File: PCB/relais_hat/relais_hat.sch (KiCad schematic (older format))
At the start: 61 parts, among them J1 Conn_01x03, J10 Conn_01x02, J11 Conn_01x02, J12 Conn_01x03, J13 DB9_Female, J14 Conn_01x02, J15 Conn_01x02, J16 Conn_01x02, J17 Conn_01x02, J18 Conn_01x02, J2 Conn_01x03, J3 Conn_02x04_Odd_Even, J4 Screw_Terminal_01x02, J5 Screw_Terminal_01x02, J6 Screw_Terminal_01x02, J7 Screw_Terminal_01x02, J8 Conn_01x02, J9 Conn_01x02, K1 RELAY-HLS8L-DC3V-S-C(5P-19X15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, K2 RELAY-HLS8L-DC3V-S-C(5P-19X15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, K3 RELAY-HLS8L-DC3V-S-C(5P-19X15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, K4 RELAY-HLS8L-DC3V-S-C(5P-19X15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, P1 Conn_02x20_Odd_Even, Q1 S8050, Q2 S8050, Q3 S8050, Q4 S8050, U1 XC6206P302MR-G, U2 XC6206P302MR-G, U3 XC6206P302MR-G, U4 XC6206P302MR-G

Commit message: ajust all board
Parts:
- D1, D2, D3, D4: footprint LED_SMD:LED_1206_3216Metric -> LED_SMD:LED_0805_2012Metric; LCSC C375461 -> C84256
- R10, R11, R12, R9: LCSC C102018 -> C17713
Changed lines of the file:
@@
 Sheet 1 1
 Title ""
-Date "15 nov 2012"
-Rev ""
+Date "2020-10-30"
+Rev "3.0"
 Comp ""
 Comment1 ""
@@
 F 0 "D2" V 4800 4550 50  0000 R CNN
 F 1 "LED" V 4700 4550 50  0000 R CNN
-F 2 "LED_SMD:LED_1206_3216Metric" H 4750 4350 50  0001 C CNN
+F 2 "LED_SMD:LED_0805_2012Metric" H 4750 4350 50  0001 C CNN
 F 3 "~" H 4750 4350 50  0001 C CNN
-F 4 "C375461" V 4750 4350 50  0001 C CNN "LCSC"
+F 4 "C84256" V 4750 4350 50  0001 C CNN "LCSC"
 	1    4750 4350
 	0    -1   -1   0
@@
 F 2 "Resistor_SMD:R_0805_2012Metric" V 4930 5300 50  0001 C CNN
 F 3 "~" H 5000 5300 50  0001 C CNN
-F 4 "C102018" V 5000 5300 50  0001 C CNN "LCSC"
+F 4 "C17713" V 5000 5300 50  0001 C CNN "LCSC"
 	1    5000 5300
 	0    -1   -1   0
@@
 F 0 "D3" V 1700 6700 50  0000 R CNN
 F 1 "LED" V 1600 6700 50  0000 R CNN
-F 2 "LED_SMD:LED_1206_3216Metric" H 1650 6500 50  0001 C CNN
+F 2 "LED_SMD:LED_0805_2012Metric" H 1650 6500 50  0001 C CNN
 F 3 "~" H 1650 6500 50  0001 C CNN
-F 4 "C375461" V 1650 6500 50  0001 C CNN "LCSC"
+F 4 "C84256" V 1650 6500 50  0001 C CNN "LCSC"
 	1    1650 6500
 	0    -1   -1   0
@@
 F 2 "Resistor_SMD:R_0805_2012Metric" V 1830 7450 50  0001 C CNN
 F 3 "~" H 1900 7450 50  0001 C CNN
-F 4 "C102018" V 1900 7450 50  0001 C CNN "LCSC"
+F 4 "C17713" V 1900 7450 50  0001 C CNN "LCSC"
 	1    1900 7450
 	0    -1   -1   0
@@
 F 0 "D1" V 1650 4700 50  0000 R CNN
 F 1 "LED" V 1550 4750 50  0000 R CNN
-F 2 "LED_SMD:LED_1206_3216Metric" H 1600 4550 50  0001 C CNN
+F 2 "LED_SMD:LED_0805_2012Metric" H 1600 4550 50  0001 C CNN
 F 3 "~" H 1600 4550 50  0001 C CNN
-F 4 "C375461" V 1600 4550 50  0001 C CNN "LCSC"
+F 4 "C84256" V 1600 4550 50  0001 C CNN "LCSC"
 	1    1600 4550
 	0    -1   -1   0
@@
 F 2 "Resistor_SMD:R_0805_2012Metric" V 1780 5500 50  0001 C CNN
 F 3 "~" H 1850 5500 50  0001 C CNN
-F 4 "C102018" V 1850 5500 50  0001 C CNN "LCSC"
+F 4 "C17713" V 1850 5500 50  0001 C CNN "LCSC"
 	1    1850 5500
 	0    -1   -1   0
@@
 F 0 "D4" V 4850 6800 50  0000 R CNN
 F 1 "LED" V 4750 6800 50  0000 R CNN
-F 2 "LED_SMD:LED_1206_3216Metric" H 4800 6600 50  0001 C CNN
+F 2 "LED_SMD:LED_0805_2012Metric" H 4800 6600 50  0001 C CNN
 F 3 "~" H 4800 6600 50  0001 C CNN
-F 4 "C375461" V 4800 6600 50  0001 C CNN "LCSC"
+F 4 "C84256" V 4800 6600 50  0001 C CNN "LCSC"
 	1    4800 6600
 	0    -1   -1   0
@@
 F 2 "Resistor_SMD:R_0805_2012Metric" V 4980 7550 50  0001 C CNN
 F 3 "~" H 5050 7550 50  0001 C CNN
-F 4 "C102018" V 5050 7550 50  0001 C CNN "LCSC"
+F 4 "C17713" V 5050 7550 50  0001 C CNN "LCSC"
 	1    5050 7550
 	0    -1   -1   0

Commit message: update ref for relais hate
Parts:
- D5, D6, D7, D8: LCSC C83528 -> C81598
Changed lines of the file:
@@
 F 2 "Diode_SMD:D_SOD-123" H 4950 4075 50  0001 C CNN
 F 3 "https://assets.nexperia.com/documents/data-sheet/1N4148_1N4448.pdf" H 4950 4250 50  0001 C CNN
-F 4 "C83528" V 4950 4250 50  0001 C CNN "LCSC"
+F 4 "C81598" V 4950 4250 50  0001 C CNN "LCSC"
 	1    4950 4250
 	0    1    1    0
@@
 F 2 "Diode_SMD:D_SOD-123" H 1850 6225 50  0001 C CNN
 F 3 "https://assets.nexperia.com/documents/data-sheet/1N4148_1N4448.pdf" H 1850 6400 50  0001 C CNN
-F 4 "C83528" V 1850 6400 50  0001 C CNN "LCSC"
+F 4 "C81598" V 1850 6400 50  0001 C CNN "LCSC"
 	1    1850 6400
 	0    1    1    0
@@
 F 2 "Diode_SMD:D_SOD-123" H 1800 4275 50  0001 C CNN
 F 3 "https://assets.nexperia.com/documents/data-sheet/1N4148_1N4448.pdf" H 1800 4450 50  0001 C CNN
-F 4 "C83528" V 1800 4450 50  0001 C CNN "LCSC"
+F 4 "C81598" V 1800 4450 50  0001 C CNN "LCSC"
 	1    1800 4450
 	0    1    1    0
@@
 F 2 "Diode_SMD:D_SOD-123" H 5000 6325 50  0001 C CNN
 F 3 "https://assets.nexperia.com/documents/data-sheet/1N4148_1N4448.pdf" H 5000 6500 50  0001 C CNN
-F 4 "C83528" V 5000 6500 50  0001 C CNN "LCSC"
+F 4 "C81598" V 5000 6500 50  0001 C CNN "LCSC"
 	1    5000 6500
 	0    1    1    0

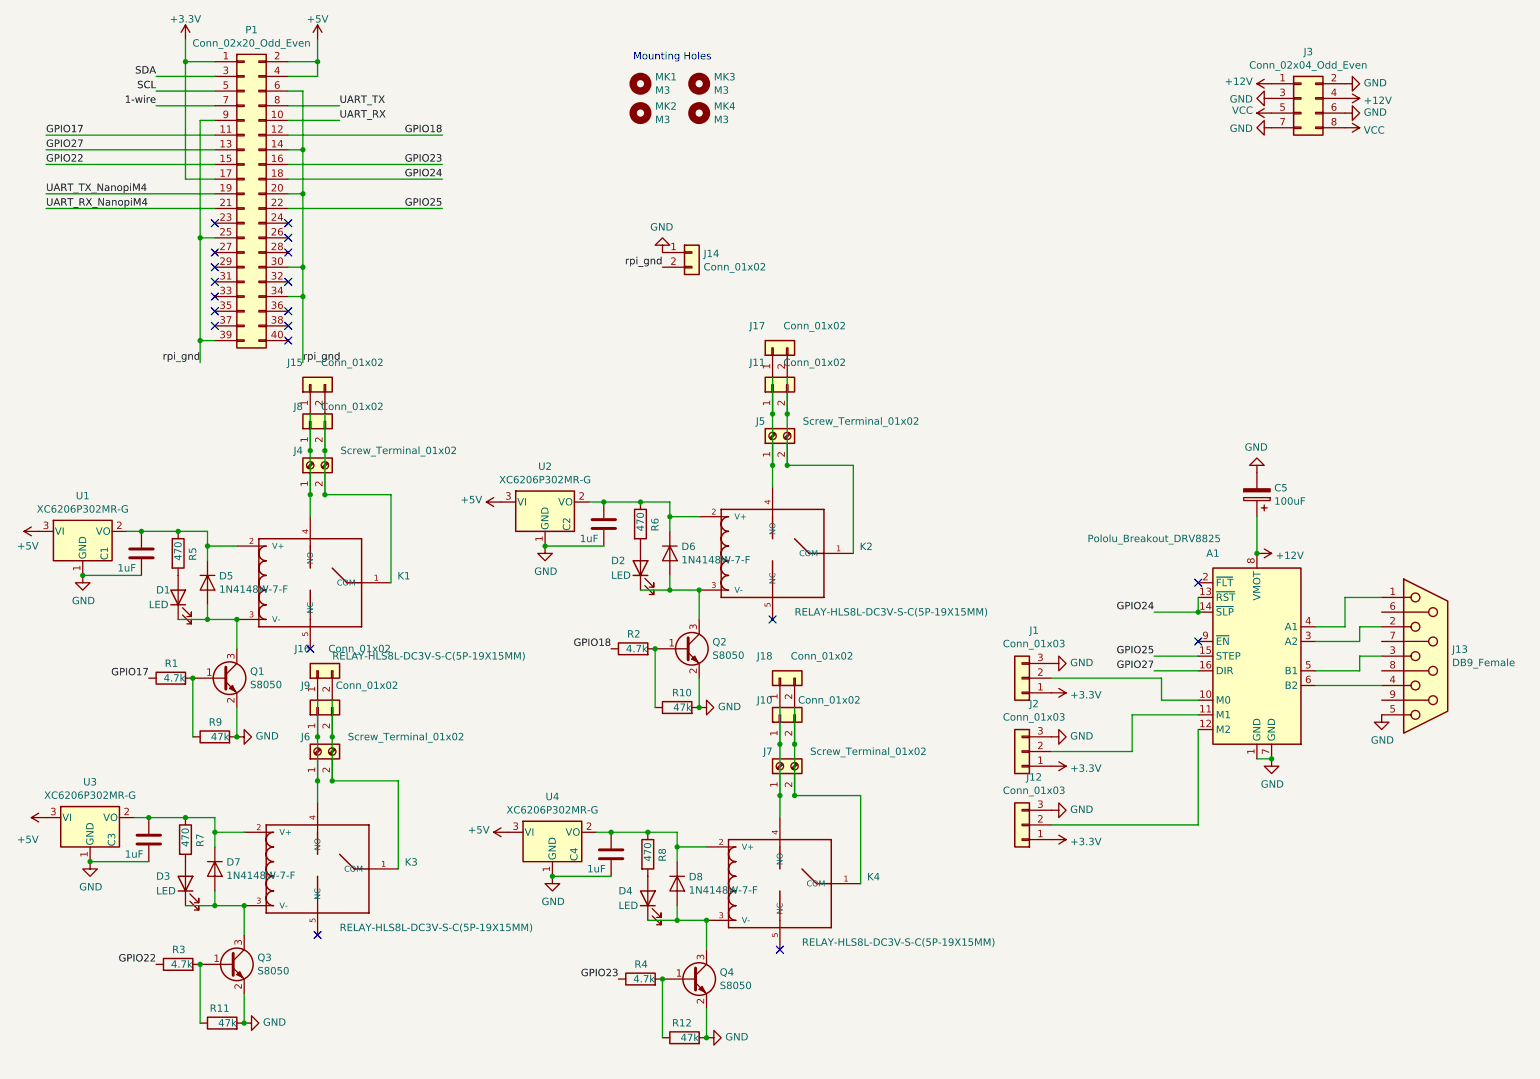
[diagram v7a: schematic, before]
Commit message: add 3D xt30 model
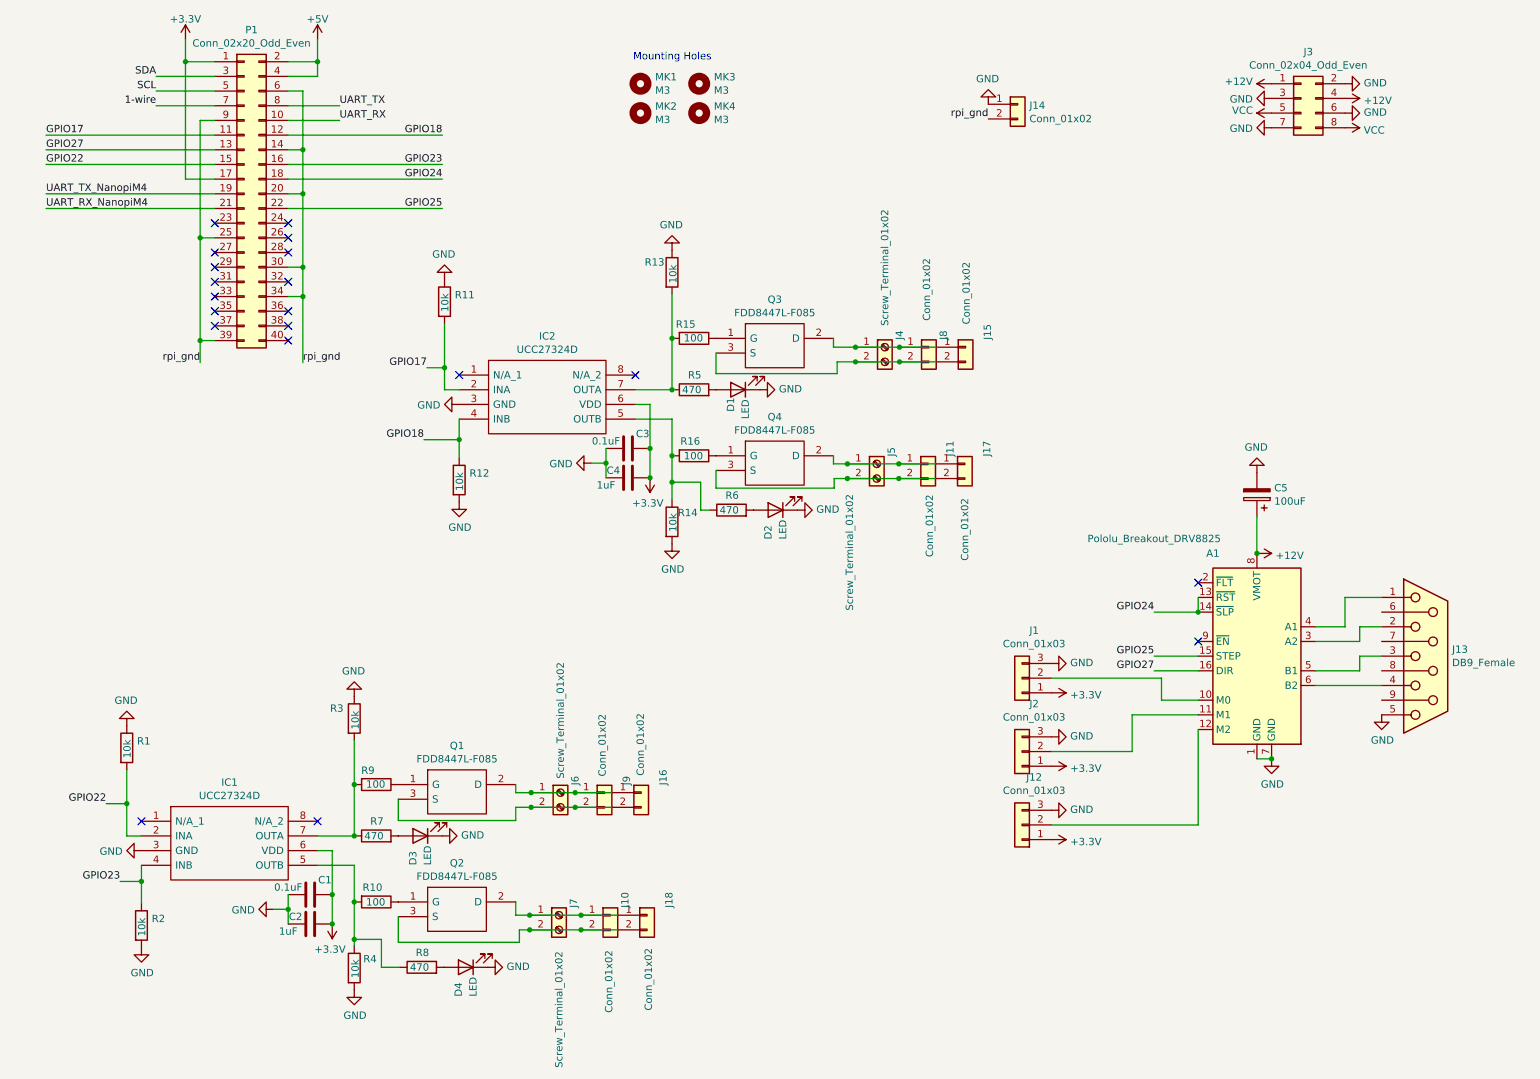
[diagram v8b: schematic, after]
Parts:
- removed D5, D6, D7, D8: 1N4148W-7-F, Diode_SMD:D_SOD-123, symbol Diode:1N4148
- removed K1, K2, K3, K4: RELAY-HLS8L-DC3V-S-C(5P-19X15MM), relais:REY5-19.0X15.0X15.0MM, symbol RELAY-HLS8L-DC3V-S-C_5P-19X15MM_:RELAY-HLS8L-DC3V-S-C(5P-19X15MM)
- removed Q1, Q2, Q3, Q4: S8050, Package_TO_SOT_SMD:SOT-23, symbol Device:Q_NPN_BEC
- removed U1, U2, U3, U4: XC6206P302MR-G, Package_TO_SOT_SMD:SOT-23, symbol Regulator_Linear:XC6206PxxxMR
- added IC1, IC2: UCC27324D, UCC27324D:SOIC127P600X175-8N, symbol UCC27324D:UCC27324D
- added Q1, Q2, Q3, Q4: FDD8447L-F085, FDD8447L:FDD8447LF085, symbol FDD8447L-F085:FDD8447L-F085
- added R13, R14: 10k, Resistor_SMD:R_0805_2012Metric, symbol Device:R
- added R15, R16: 100, Resistor_SMD:R_0805_2012Metric, symbol Device:R
- C1, C3: value 1uF -> 0.1uF; LCSC C28323 -> C49678
- R1, R2, R3, R4: value 4.7k -> 10k; LCSC C17673 -> C17414
- R10: value 47k -> 100; LCSC C17713 -> C17408
- R11, R12: value 47k -> 10k; LCSC C17713 -> C17414
- R9: value 47k -> 100; LCSC C17713 -> C17414
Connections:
- net +3V3: now also C1.1, C2.1, C3.1, C4.1, IC1.6 (VDD), IC2.6 (VDD)
- net GND: now also D1.1 (K), D2.1 (K), D3.1 (K), D4.1 (K), R1.1, R11.1, R2.2, R3.1, R4.2, IC1.3 (GND), IC2.3 (GND), R13.1, R14.2; no longer R10.2, R11.2, R9.2
- net GPIO17: now also R11.2, IC2.2 (INA); no longer R1.1
- net GPIO18: now also R12.1, IC2.4 (INB); no longer R2.1
- net GPIO22: now also R1.2, IC1.2 (INA); no longer R3.1
- net GPIO23: now also R2.1, IC1.4 (INB); no longer R4.1
- net at J16.1 (Pin_1), J6.1 (Pin_1), J9.1 (Pin_1): now also Q1.2 (D)
- net at J16.2 (Pin_2), J6.2 (Pin_2), J9.2 (Pin_2): now also Q1.3 (S)
- net at J15.1 (Pin_1), J4.1 (Pin_1), J8.1 (Pin_1): now also Q3.2 (D)
- net at J15.2 (Pin_2), J4.2 (Pin_2), J8.2 (Pin_2): now also Q3.3 (S)
- net at J10.1 (Pin_1), J18.1 (Pin_1), J7.1 (Pin_1): now also Q2.2 (D)
- net at J10.2 (Pin_2), J18.2 (Pin_2), J7.2 (Pin_2): now also Q2.3 (S)
- net at J11.1 (Pin_1), J17.1 (Pin_1), J5.1 (Pin_1): now also Q4.2 (D)
- net at J11.2 (Pin_2), J17.2 (Pin_2), J5.2 (Pin_2): now also Q4.3 (S)
- net at R6.1: now also IC2.5 (OUTB), R14.1, R16.2; no longer C2.1
- net at R10.1: now also Q2.1 (G); no longer R2.2
- net at R7.1: now also R3.2, R9.2, IC1.7 (OUTA); no longer C3.1
- net at R5.1: now also IC2.7 (OUTA), R13.2, R15.2; no longer C1.1
- net at R9.1: now also Q1.1 (G); no longer R1.2
- net at R8.1: now also R10.2, R4.1, IC1.5 (OUTB); no longer C4.1
- new net: Q3.1 (G), R15.1
- new net: Q4.1 (G), R16.1
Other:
- moved on the sheet: D1, D2, D3, D4, J10, J11, J14, J15, J16, J17, J18, J4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
